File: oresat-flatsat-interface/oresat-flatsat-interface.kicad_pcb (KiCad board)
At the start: 4 copper layers, 99.8 x 109.6 mm, 11 parts, among them J1 J-SAMTEC-TFM-120-01-L-D-RA, J10 Conn_01x20, J2 733000020, J3 733000020, J4 733000020, J5 Conn_Coaxial, J6 Conn_Coaxial, J7 Conn_Coaxial, J8 J-SAMTEC-TFM-110-01-L-D-RA, J9 Conn_01x40

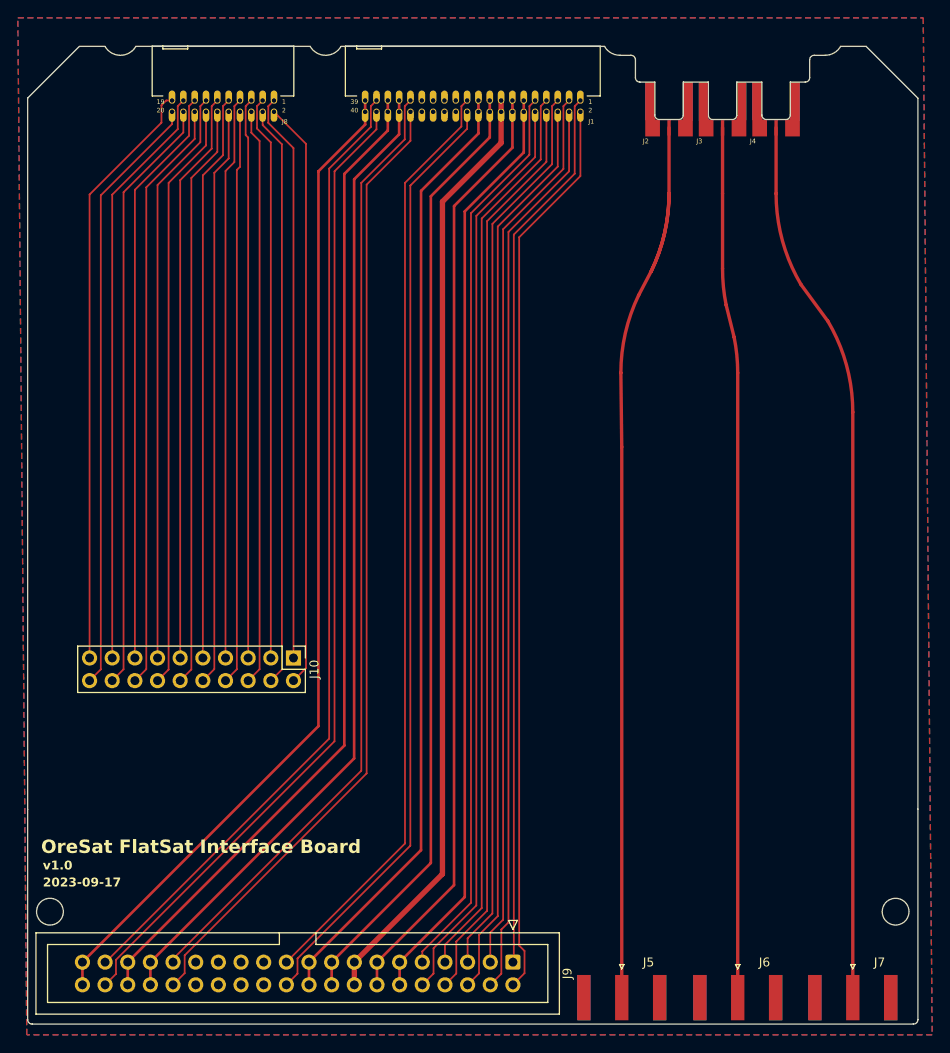
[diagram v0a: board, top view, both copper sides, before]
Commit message: Updated oresat-flatsat interface RF traces and finished cleaning up
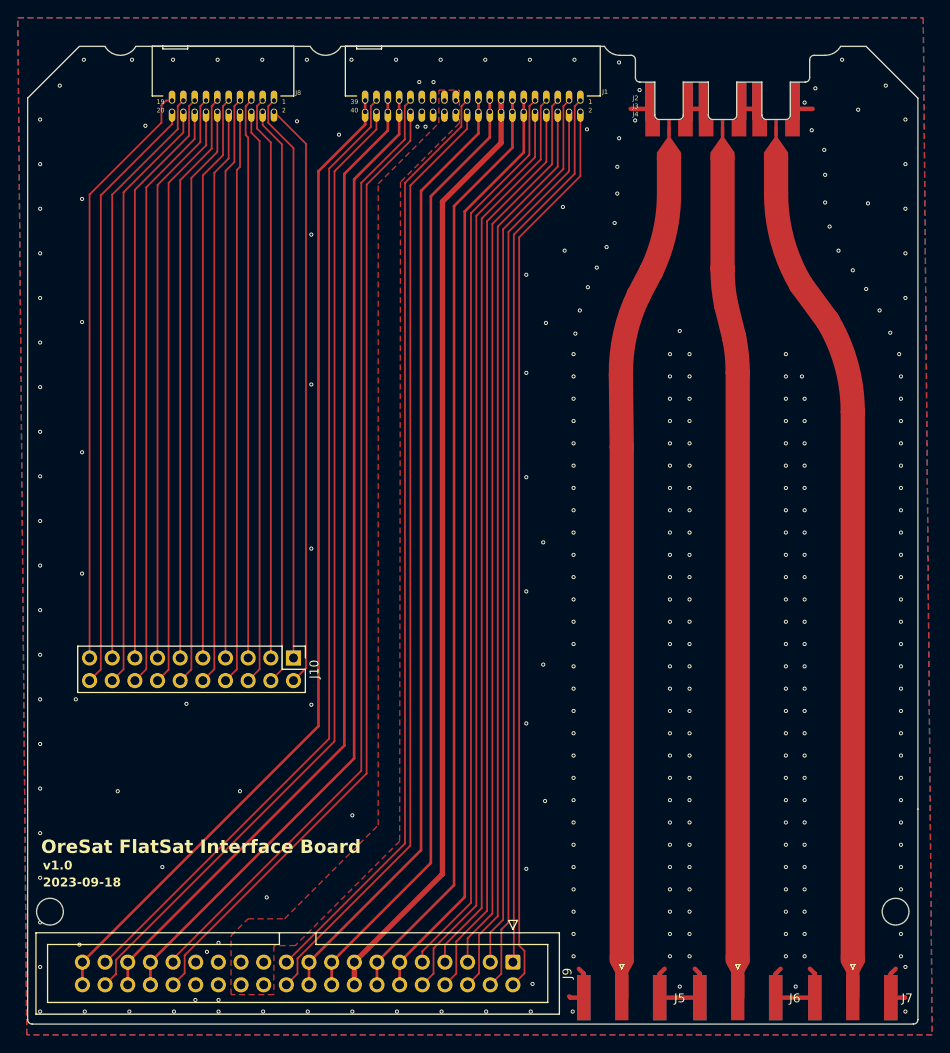
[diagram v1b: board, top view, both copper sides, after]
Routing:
- net GND: track 0.00 -> 40.5 mm, vias 0 -> 291
- added copper zone on F.Cu, net VBUS
- removed copper zone on In1.Cu, net GND
- removed copper zone on In2.Cu, net GND
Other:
- copper layers 4 -> 2
- board text added: "2023-09-18"
- board text removed: "2023-09-17"
